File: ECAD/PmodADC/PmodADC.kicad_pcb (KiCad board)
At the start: 4 copper layers, 142 parts, among them J1 AudioIn, J3 Pmod, J4 AudioOut, SW1 Bypass, SW2 Bypass, U1 74VHCT595BQ-Q100, U10 LM337_SOT223, U11 TLV172IDCK, U12 74VHCT595BQ-Q100, U13 74VHCT595BQ-Q100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

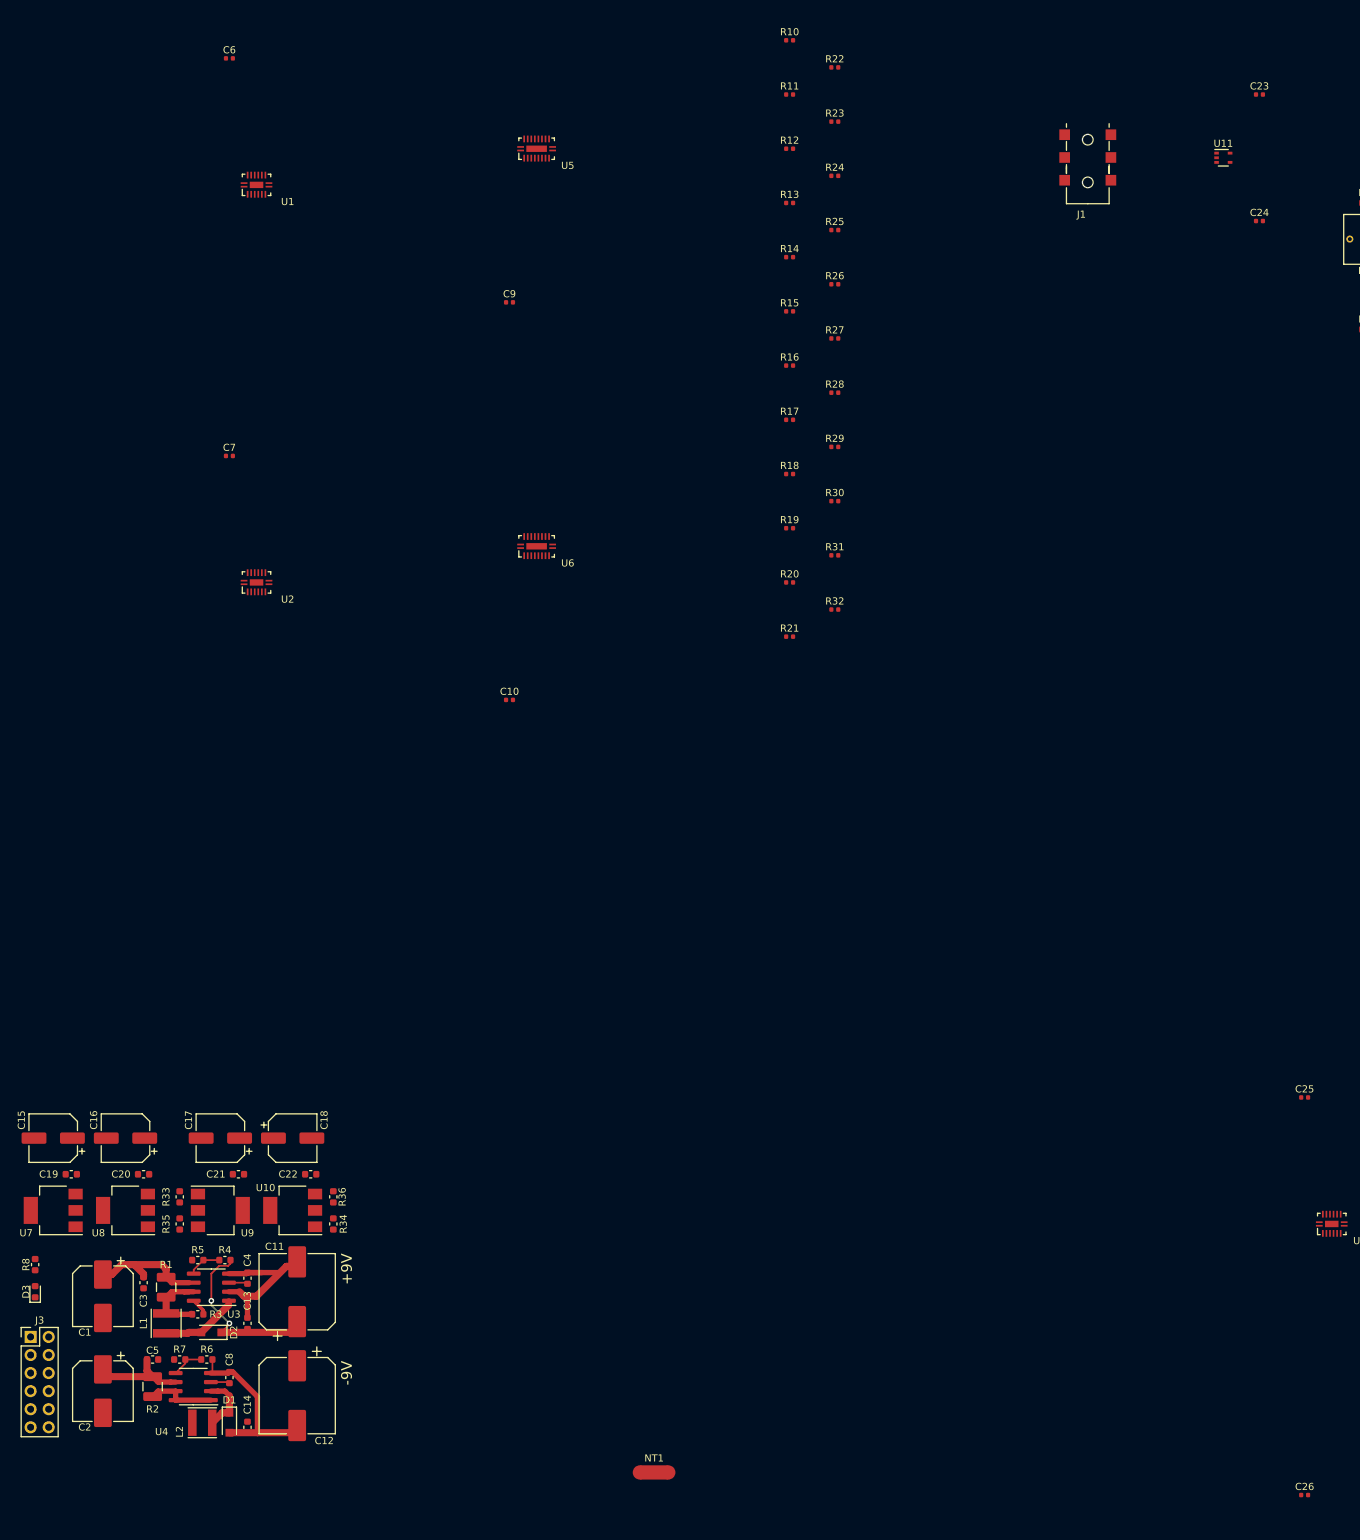
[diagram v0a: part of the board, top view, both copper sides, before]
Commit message: Reworked Power Scheme
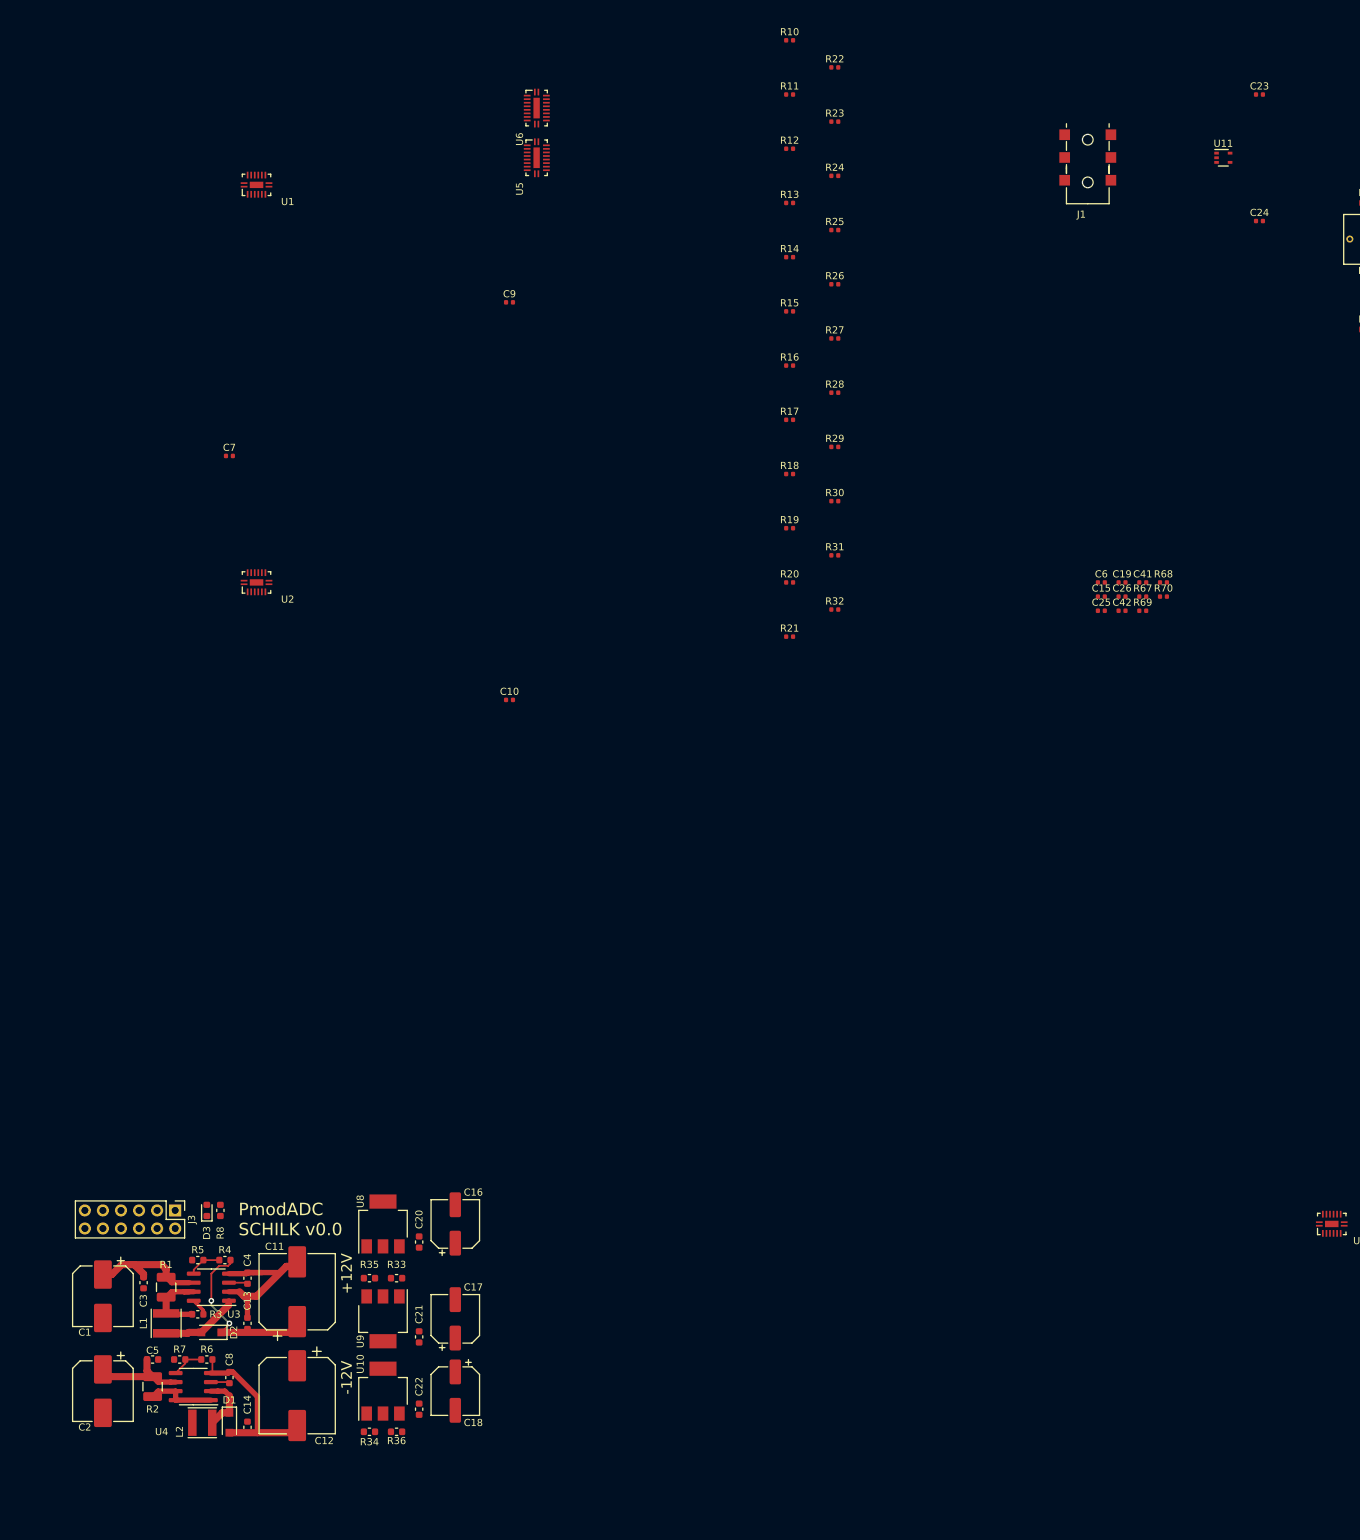
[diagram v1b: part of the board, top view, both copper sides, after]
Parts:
- removed NT1: AGND, NetTie:NetTie-2_SMD_Pad2.0mm
- removed U7: L7805, Package_TO_SOT_SMD:SOT-223
- added C41: 1u, Capacitor_SMD:C_0402_1005Metric, F.Cu at (118.8, -214.6)
- added C42: 100n, Capacitor_SMD:C_0402_1005Metric, F.Cu at (115.9, -210.7)
- added R67: 100R, Resistor_SMD:R_0402_1005Metric, F.Cu at (118.8, -212.6)
- added R68: 100R, Resistor_SMD:R_0402_1005Metric, F.Cu at (121.8, -214.6)
- added R69: 100R, Resistor_SMD:R_0402_1005Metric, F.Cu at (118.8, -210.7)
- added R70: 100R, Resistor_SMD:R_0402_1005Metric, F.Cu at (121.8, -212.6)
- C15: value 10u -> 100n; footprint Capacitor_SMD:CP_Elec_6.3x7.7 -> Capacitor_SMD:C_0402_1005Metric
- C19: value 100n -> 1u; footprint Capacitor_SMD:C_0603_1608Metric -> Capacitor_SMD:C_0402_1005Metric
- C25, C6: value 100n -> 1u
- C4: value 120pf -> 470p
- R4, R6: value 10K -> TODO
- R5, R7: value 56K -> TODO
- moved C19 169.5 mm to (115.9, -214.6), turned to 0 degrees
- moved C15 165.8 mm to (113.0, -212.6), turned to 0 degrees
- moved C6 143.0 mm to (113.0, -214.6)
- moved C26 128.9 mm to (115.9, -212.6)
- moved C25 74.1 mm to (113.0, -210.7)
- moved U6 61.6 mm to (33.7, -281.3), turned to 270 degrees
- moved C16 47.9 mm to (22.2, -124.5), turned to 90 degrees
- moved C18 42.3 mm to (22.2, -101.0), turned to 270 degrees
- moved C17 41.7 mm to (22.2, -111.1), turned to 90 degrees
- moved C20 39.9 mm to (17.1, -121.9), turned to 90 degrees
- moved C22 36.4 mm to (17.1, -98.4), turned to 270 degrees
- moved U8 36.2 mm to (12.1, -124.5), turned to 90 degrees
- moved R36 34.2 mm to (14.0, -95.2), turned to 180 degrees
- moved C21 34.2 mm to (17.1, -108.6), turned to 90 degrees
- moved R33 32.6 mm to (14.0, -116.8), turned to 180 degrees
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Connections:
- C10 pad 1: +5VA -> +5V
- C10 pad 2: GNDA -> GND
- C15 pad 1: +5V -> Net-(C15-Pad1)
- C16 pad 1: +5VA -> +5V
- C16 pad 2: GNDA -> GND
- C17 pad 2: Net-(C17-Pad2) -> GND
- C18 pad 1: Net-(C17-Pad2) -> GND
- C19 pad 1: +5V -> Net-(C19-Pad1)
- C20 pad 1: +5VA -> +5V
- C20 pad 2: GNDA -> GND
- C21 pad 2: Net-(C17-Pad2) -> GND
- C22 pad 1: Net-(C17-Pad2) -> GND
- C23 pad 1: GNDA -> GND
- C24 pad 1: GNDA -> GND
- C25 pad 1: +5V -> Net-(C25-Pad1)
- C26 pad 1: +5V -> Net-(C25-Pad1)
- C28 pad 1: +5VA -> +5V
- C28 pad 2: GNDA -> GND
- C29 pad 1: +5VA -> +5V
- C29 pad 2: GNDA -> GND
- C30 pad 2: GNDA -> GND
- C31 pad 2: GNDA -> GND
- C32 pad 2: GNDA -> GND
- C33 pad 2: GNDA -> GND
- C34 pad 2: GNDA -> GND
- C35 pad 1: GNDA -> GND
- C36 pad 1: GNDA -> GND
- C38 pad 1: GNDA -> GND
- C39 pad 1: GNDA -> GND
- C40 pad 1: +5VA -> +5V
- C40 pad 2: GNDA -> GND
- C6 pad 1: +5V -> Net-(C15-Pad1)
- C7 pad 1: +5V -> Net-(C19-Pad1)
- C9 pad 1: +5VA -> +5V
- C9 pad 2: GNDA -> GND
- J1 pad S: GNDA -> GND
- J4 pad S: GNDA -> GND
- R33 pad 1: GNDA -> GND
- R34 pad 2: GNDA -> GND
- R38 pad 2: GNDA -> GND
- R39 pad 1: +5VA -> +5V
- R40 pad 2: GNDA -> GND
- R41 pad 2: GNDA -> GND
- R65 pad 1: GNDA -> GND
- R9 pad 2: GNDA -> GND
- RV3 pad 3: GNDA -> GND
- SW1 pad 4: (no net) -> Net-(SW1-Pad4)
- SW1 pad 5: (no net) -> Net-(SW1-Pad5)
- SW1 pad 6: (no net) -> Net-(SW1-Pad6)
- SW2 pad 4: (no net) -> Net-(SW2-Pad4)
- SW2 pad 5: (no net) -> Net-(SW2-Pad5)
- SW2 pad 6: (no net) -> Net-(SW2-Pad6)
- U1 pad 16: +5V -> Net-(C15-Pad1)
- U12 pad 16: +5V -> Net-(C25-Pad1)
- U13 pad 16: +5V -> Net-(C41-Pad1)
- U13 pad 4: (no net) -> Net-(U13-Pad4)
- U13 pad 5: (no net) -> Net-(U13-Pad5)
- U13 pad 6: (no net) -> Net-(U13-Pad6)
- U13 pad 7: (no net) -> Net-(U13-Pad7)
- U13 pad 9: (no net) -> Net-(U13-Pad9)
- U14 pad 1: GNDA -> GND
- U14 pad 10: GNDA -> GND
- U14 pad 19: GNDA -> GND
- U14 pad 20: +5VA -> +5V
- U15 pad 1: GNDA -> GND
- U15 pad 10: GNDA -> GND
- U15 pad 15: (no net) -> Net-(U15-Pad15)
- U15 pad 16: (no net) -> Net-(U15-Pad16)
- U15 pad 17: (no net) -> Net-(U15-Pad17)
- U15 pad 18: (no net) -> Net-(U15-Pad18)
- U15 pad 19: GNDA -> GND
- U15 pad 2: GNDA -> GND
- U15 pad 20: +5VA -> +5V
- U15 pad 3: GNDA -> GND
- U15 pad 4: GNDA -> GND
- U15 pad 5: GNDA -> GND
- U16 pad 7: GNDA -> GND
- U19 pad 2: GNDA -> GND
- U19 pad 5: +5VA -> +5V
- U2 pad 16: +5V -> Net-(C19-Pad1)
- U2 pad 4: (no net) -> Net-(U2-Pad4)
- U2 pad 5: (no net) -> Net-(U2-Pad5)
- U2 pad 6: (no net) -> Net-(U2-Pad6)
- U2 pad 7: (no net) -> Net-(U2-Pad7)
- U2 pad 9: (no net) -> Net-(U2-Pad9)
- U5 pad 1: GNDA -> GND
- U5 pad 10: GNDA -> GND
- U5 pad 19: GNDA -> GND
- U5 pad 20: +5VA -> +5V
- U6 pad 1: GNDA -> GND
- U6 pad 10: GNDA -> GND
- U6 pad 15: (no net) -> Net-(U6-Pad15)
- U6 pad 16: (no net) -> Net-(U6-Pad16)
- U6 pad 17: (no net) -> Net-(U6-Pad17)
- U6 pad 18: (no net) -> Net-(U6-Pad18)
- U6 pad 19: GNDA -> GND
- U6 pad 2: GNDA -> GND
- U6 pad 20: +5VA -> +5V
- U6 pad 3: GNDA -> GND
- U6 pad 4: GNDA -> GND
- U6 pad 5: GNDA -> GND
- U8 pad 2: GNDA -> GND
- U8 pad 3: +5VA -> +5V
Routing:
- net GNDA: track 2.57 -> 0.00 mm
- net GND: track 26.6 -> 29.2 mm
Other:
- board text added: "+12V"
- board text added: "-12V"
- board text added: "PmodADC SCHILK v0.0"
- board text removed: "+9V"
- board text removed: "-9V"

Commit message: PCB v0.0 Done.
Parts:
- added C43: 100n, Capacitor_SMD:C_0402_1005Metric, F.Cu at (-10.2, -85.7)
- added C44: 100n, Capacitor_SMD:C_0402_1005Metric, F.Cu at (-4.45, -85.7)
- added J2: LeaderTech SMS405, Leader_SMS405:Leader_SMS405, F.Cu at (-13.3, -89.5)
- added JP1: BitSelect, Jumper:SolderJumper-3_P1.3mm_Open_RoundedPad1.0x1.5mm, F.Cu at (5.08, -81.3)
- added JP2: Bypass, Jumper:SolderJumper-3_P1.3mm_Open_RoundedPad1.0x1.5mm, F.Cu at (18.4, -75.6)
- added JP3: BitSelect, Jumper:SolderJumper-3_P1.3mm_Open_RoundedPad1.0x1.5mm, F.Cu at (-15.2, -87.0)
- added JP4: Vref_Feedback, Jumper:SolderJumper-3_P1.3mm_Open_RoundedPad1.0x1.5mm, F.Cu at (-1.27, -85.1)
- added R71: 20K 0.1%, Resistor_SMD:R_0402_1005Metric, F.Cu at (0.00, -81.9)
- added R72: 20K 0.1%, Resistor_SMD:R_0402_1005Metric, F.Cu at (0.00, -83.2)
- added R73: 10K 0.1%, Resistor_SMD:R_0402_1005Metric, F.Cu at (2.54, -81.9)
- added R74: 10K 0.1%, Resistor_SMD:R_0402_1005Metric, F.Cu at (2.54, -83.2)
- added R75: 20K 0.1%, Resistor_SMD:R_0402_1005Metric, F.Cu at (-20.3, -87.6)
- added R76: 20K 0.1%, Resistor_SMD:R_0402_1005Metric, F.Cu at (-20.3, -88.9)
- added R77: 10K 0.1%, Resistor_SMD:R_0402_1005Metric, F.Cu at (-17.8, -87.6)
- added R78: 10K 0.1%, Resistor_SMD:R_0402_1005Metric, F.Cu at (-17.8, -88.9)
- added TP10: S&H, TestPoint:TestPoint_Pad_D1.0mm, F.Cu at (22.2, -85.7)
- added TP11: S&H_o, TestPoint:TestPoint_Pad_D1.0mm, F.Cu at (22.2, -75.6)
- added TP12: GND, TestPoint:TestPoint_Pad_D1.0mm, F.Cu at (22.2, -83.2)
- added TP13: DAC, TestPoint:TestPoint_Pad_D1.0mm, F.Cu at (-15.2, -82.5)
- added TP14: OUT1, TestPoint:TestPoint_Pad_D1.0mm, F.Cu at (-29.2, -59.1)
- added TP15: GND, TestPoint:TestPoint_Pad_D1.0mm, F.Cu at (18.4, -70.5)
- added TP16: OUT2, TestPoint:TestPoint_Pad_D1.0mm, F.Cu at (-15.2, -60.3)
- added TP18: OUT, TestPoint:TestPoint_Pad_D1.0mm, F.Cu at (-11.4, -60.3)
- added TP19: GND, TestPoint:TestPoint_Pad_D1.0mm, F.Cu at (-15.2, -80.0)
- added TP4: GND, TestPoint:TestPoint_Pad_D1.0mm, F.Cu at (5.08, -74.3)
- added TP5: DAC, TestPoint:TestPoint_Pad_D1.0mm, F.Cu at (5.08, -76.8)
- added TP6: PREA, TestPoint:TestPoint_Pad_D1.0mm, F.Cu at (-4.45, -50.2)
- added TP7: IN, TestPoint:TestPoint_Pad_D1.0mm, F.Cu at (-4.45, -52.7)
- added TP9: S&H_i, TestPoint:TestPoint_Pad_D1.0mm, F.Cu at (14.6, -75.6)
- added U7: MAX6071BAUT50+T, Package_TO_SOT_SMD:SOT-23-6, F.Cu at (-7.45, -84.8)
- R4, R6: value TODO -> 12K
- R5, R7: value TODO -> 1K5
- R66: footprint Resistor_SMD:R_0603_1608Metric -> Resistor_SMD:R_0402_1005Metric
- moved J4 364.4 mm to (-22.2, -51.4), turned to 180 degrees
- moved R66 345.7 mm to (8.26, -71.1)
- moved TP3 343.2 mm to (8.26, -68.6), turned to 180 degrees
- moved SW2 340.9 mm to (-14.6, -56.5)
- moved C38 335.5 mm to (-29.8, -68.6), turned to 90 degrees
- moved C40 334.0 mm to (11.4, -71.1), turned to 180 degrees
- moved C39 330.5 mm to (-26.0, -68.6), turned to 270 degrees
- moved U19 328.8 mm to (11.4, -69.2)
- moved U18 327.8 mm to (-27.9, -68.6), turned to 90 degrees
- moved TP1 314.9 mm to (14.6, -66.7)
- moved TP2 309.9 mm to (14.6, -70.5)
- moved RV3 304.9 mm to (-19.7, -65.4)
- moved C37 303.0 mm to (-21.6, -62.9), turned to 180 degrees
- moved C35 296.1 mm to (-29.8, -63.5), turned to 90 degrees
- moved C36 289.9 mm to (-26.0, -63.5), turned to 270 degrees
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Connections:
- C10 pad 1: +5V -> /Vref_5V
- C28 pad 1: +5V -> /Vref_5V
- C29 pad 1: +5V -> /Vref_5V
- C9 pad 1: +5V -> /Vref_5V
- R21 pad 1: Net-(R21-Pad1) -> Net-(JP1-Pad3)
- R32 pad 2: Net-(R21-Pad1) -> Net-(JP1-Pad3)
- R53 pad 1: Net-(R53-Pad1) -> Net-(JP3-Pad3)
- R64 pad 2: Net-(R53-Pad1) -> Net-(JP3-Pad3)
- TP1 pad 1: Net-(TP1-Pad1) -> Net-(JP2-Pad2)
- TP2 pad 1: Net-(R21-Pad1) -> Net-(JP1-Pad2)
- U14 pad 20: +5V -> /Vref_5V
- U15 pad 20: +5V -> /Vref_5V
- U15 pad 4: GND -> Net-(U13-Pad5)
- U15 pad 5: GND -> Net-(U13-Pad4)
- U16 pad 5: Net-(TP1-Pad1) -> Net-(JP2-Pad1)
- U17 pad 1: Net-(R53-Pad1) -> Net-(JP3-Pad2)
- U19 pad 3: Net-(TP1-Pad1) -> Net-(JP2-Pad2)
- U19 pad 4: Net-(R21-Pad1) -> Net-(JP1-Pad2)
- U5 pad 20: +5V -> /Vref_5V
- U6 pad 18: Net-(U6-Pad18) -> /Vref_Sense
- U6 pad 2: GND -> +5V
- U6 pad 20: +5V -> /Vref_5V
- U6 pad 4: GND -> Net-(U2-Pad5)
- U6 pad 5: GND -> Net-(U2-Pad4)
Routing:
- net GND: track 29.2 -> 431.0 mm, vias 0 -> 87
- net +9V: track 0.00 -> 232.3 mm, vias 0 -> 10
- net +5V: track 0.00 -> 210.8 mm, vias 0 -> 13
- net -9V: track 0.00 -> 164.2 mm, vias 0 -> 7
- net +3V3: track 30.4 -> 145.9 mm, vias 0 -> 6
- net /COMP: track 0.00 -> 92.6 mm, vias 0 -> 2
- net /S&H: track 0.00 -> 85.5 mm, vias 0 -> 2
- net /DAC_L: track 0.00 -> 71.0 mm, vias 0 -> 2
- net /DAC_C: track 0.00 -> 66.7 mm, vias 0 -> 2
- net /ADC_C: track 0.00 -> 66.0 mm, vias 0 -> 2
- net /ADC_S: track 0.00 -> 65.6 mm, vias 0 -> 1
- net /DAC_S: track 0.00 -> 61.6 mm, vias 0 -> 2
- net /Vref_5V: track 0.00 -> 59.7 mm, vias 0 -> 5
- net /ADC_L: track 0.00 -> 59.5 mm, vias 0 -> 2
- net Net-(J1-PadT): track 0.00 -> 43.1 mm
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- added copper zone on In1.Cu, net GND
- added copper zone on In2.Cu, net GND
- added copper zone on In1.Cu, net Net-(JP2-Pad1)
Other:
- board outline added: 59.1 x 80 mm
- board text added: "+5V"
- board text added: "+9V"
- board text added: "-9V"
- board text added: "14bit DAC:"
- board text added: "14bit SAR ADC:"
- board text added: "Comp"
- board text added: "DAC"
- board text added: "IN"
- board text added: "OUT"
- board text added: "REF"
- board text added: "S&H"
